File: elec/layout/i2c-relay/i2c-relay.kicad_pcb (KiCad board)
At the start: 2 copper layers, 7 parts, among them U2 10kΩ ±1% 62.5mW, U3 1kΩ ±1% 62.5mW

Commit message: Build everything with ordered params to fix frozen builds
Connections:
- net RESET renamed VCCP
- Q1 pad 2: gnd -> gnd-2
- U1 pad 10: gpio_expander-net-5 -> gpio_expander-net-3
- U1 pad 17: gnd-2 -> gnd
- U1 pad 3: gpio_expander-net-1 -> gpio_expander-net-2
- U1 pad 4: gpio_expander-net-6 -> gpio_expander-net
- U1 pad 5: gpio_expander-net -> gpio_expander-net-6
- U1 pad 6: gnd-2 -> gnd
- U1 pad 7: gpio_expander-net-3 -> gpio_expander-net-5
- U1 pad 9: gpio_expander-net-2 -> gpio_expander-net-1
- U3 pad 2: gnd -> gnd-2
- U4 pad 2: hv -> hv-1
- U6 pad 1: hv -> hv-1
- U6 pad 5: hv-1 -> hv-2
- U6 pad 6: hv-2 -> hv
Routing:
- net hv-1: track 0.00 -> 2.39 mm
- net hv: track 2.39 -> 0.00 mm
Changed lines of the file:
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@@
     )
     (net 0 "")
-    (net 1 "gpio_expander-net-6")
+    (net 1 "gpio_expander-net")
     (net 2 "SCL")
-    (net 3 "gpio_expander-net-5")
-    (net 4 "hv-2")
-    (net 5 "gpio_expander-net-3")
-    (net 6 "gpio_expander-net-2")
-    (net 7 "hv")
+    (net 3 "gpio_expander-net-3")
+    (net 4 "hv")
+    (net 5 "gpio_expander-net-5")
+    (net 6 "gpio_expander-net-1")
+    (net 7 "hv-1")
     (net 8 "line")
     (net 9 "gnd-1")
     (net 10 "INT")
     (net 11 "gpio_expander-net-4")
-    (net 12 "RESET")
-    (net 13 "hv-1")
+    (net 12 "VCCP")
+    (net 13 "hv-2")
     (net 14 "SDA")
-    (net 15 "gpio_expander-net")
+    (net 15 "gpio_expander-net-6")
     (net 16 "gnd-3")
-    (net 17 "gnd")
+    (net 17 "gnd-2")
     (net 18 "gate")
-    (net 19 "gpio_expander-net-1")
-    (net 20 "gnd-2")
+    (net 19 "gpio_expander-net-2")
+    (net 20 "gnd")
     (net 21 "relay-gnd")
     (net 22 "cathode")
@@
             )
         )
+        (property "PARAM_max_power" "{\"type\": \"Quantity_Set_Discrete\", \"data\": {\"intervals\": {\"type\": \"Numeric_Interval_Disjoint\", \"data\": {\"intervals\": [{\"type\": \"Numeric_Interval\", \"data\": {\"min\": 0.0625, \"max\": 0.0625}}]}}, \"unit\": \"watt\"}}"
+            (at 0 0 0)
+            (layer "User.9")
+            (hide yes)
+            (effects
+                (font
+                    (size 0.125 0.125)
+                    (thickness 0.01875)
+                )
+            )
+        )
+        (property "PARAM_max_voltage" "{\"type\": \"Quantity_Set_Discrete\", \"data\": {\"intervals\": {\"type\": \"Numeric_Interval_Disjoint\", \"data\": {\"intervals\": [{\"type\": \"Numeric_Interval\", \"data\": {\"min\": 50.0, \"max\": 50.0}}]}}, \"unit\": \"volt\"}}"
+            (at 0 0 0)
+            (layer "User.9")
+            (hide yes)
+            (effects
+                (font
+                    (size 0.125 0.125)
+                    (thickness 0.01875)
+                )
+            )
+        )
+        (property "PARAM_resistance" "{\"type\": \"Quantity_Interval_Disjoint\", \"data\": {\"intervals\": {\"type\": \"Numeric_Interval_Disjoint\", \"data\": {\"intervals\": [{\"type\": \"Numeric_Interval\", \"data\": {\"min\": 990.0000002235174, \"max\": 1009.9999997764826}}]}}, \"unit\": \"ohm\"}}"
+            (at 0 0 0)
+            (layer "User.9")
+            (hide yes)
+            (effects
+                (font
+                    (size 0.125 0.125)
+                    (thickness 0.01875)
+                )
+            )
+        )
         (attr smd)
         (fp_line
@@
             (size 0.57 0.54)
             (layers "F.Cu" "F.Mask" "F.Paste")
-            (net 17 "gnd")
+            (net 17 "gnd-2")
             (remove_unused_layers yes)
             (keep_end_layers yes)
@@
             (size 0.8 0.8)
             (layers "F.Cu" "F.Mask" "F.Paste")
-            (net 7 "hv")
+            (net 7 "hv-1")
             (remove_unused_layers yes)
             (keep_end_layers yes)
@@
             (drill 0.999998)
             (layers "*.Cu" "*.Mask")
-            (net 7 "hv")
+            (net 7 "hv-1")
             (remove_unused_layers no)
             (keep_end_layers yes)
@@
             (drill 0.999998)
             (layers "*.Cu" "*.Mask")
-            (net 13 "hv-1")
+            (net 13 "hv-2")
             (remove_unused_layers no)
             (keep_end_layers yes)
@@
             (drill 0.999998)
             (layers "*.Cu" "*.Mask")
-            (net 4 "hv-2")
+            (net 4 "hv")
             (remove_unused_layers no)
             (keep_end_layers yes)
@@
             )
         )
+        (property "PARAM_max_power" "{\"type\": \"Quantity_Set_Discrete\", \"data\": {\"intervals\": {\"type\": \"Numeric_Interval_Disjoint\", \"data\": {\"intervals\": [{\"type\": \"Numeric_Interval\", \"data\": {\"min\": 0.0625, \"max\": 0.0625}}]}}, \"unit\": \"watt\"}}"
+            (at 0 0 0)
+            (layer "User.9")
+            (hide yes)
+            (effects
+                (font
+                    (size 0.125 0.125)
+                    (thickness 0.01875)
+                )
+            )
+        )
+        (property "PARAM_resistance" "{\"type\": \"Quantity_Interval_Disjoint\", \"data\": {\"intervals\": {\"type\": \"Numeric_Interval_Disjoint\", \"data\": {\"intervals\": [{\"type\": \"Numeric_Interval\", \"data\": {\"min\": 990.0000002235174, \"max\": 1009.9999997764826}}]}}, \"unit\": \"ohm\"}}"
+            (at 0 0 0)
+            (layer "User.9")
+            (hide yes)
+            (effects
+                (font
+                    (size 0.125 0.125)
+                    (thickness 0.01875)
+                )
+            )
+        )
+        (property "PARAM_max_voltage" "{\"type\": \"Quantity_Set_Discrete\", \"data\": {\"intervals\": {\"type\": \"Numeric_Interval_Disjoint\", \"data\": {\"intervals\": [{\"type\": \"Numeric_Interval\", \"data\": {\"min\": 50.0, \"max\": 50.0}}]}}, \"unit\": \"volt\"}}"
+            (at 0 0 0)
+            (layer "User.9")
+            (hide yes)
+            (effects
+                (font
+                    (size 0.125 0.125)
+                    (thickness 0.01875)
+                )
+            )
+        )
         (attr smd)
         (fp_line
@@
             (size 1.07 0.6)
             (layers "F.Cu" "F.Paste" "F.Mask")
-            (net 17 "gnd")
+            (net 17 "gnd-2")
             (remove_unused_layers yes)
             (keep_end_layers yes)
@@
             (size 0.28 0.66)
             (layers "F.Cu" "F.Mask" "F.Paste")
-            (net 12 "RESET")
+            (net 12 "VCCP")
             (remove_unused_layers yes)
             (keep_end_layers yes)
@@
             (size 0.28 0.66)
             (layers "F.Cu" "F.Mask" "F.Paste")
-            (net 19 "gpio_expander-net-1")
+            (net 19 "gpio_expander-net-2")
             (remove_unused_layers yes)
             (keep_end_layers yes)
@@
             (size 0.28 0.66)
             (layers "F.Cu" "F.Mask" "F.Paste")
-            (net 1 "gpio_expander-net-6")
+            (net 1 "gpio_expander-net")
             (remove_unused_layers yes)
             (keep_end_layers yes)
@@
             (size 0.66 0.28)
             (layers "F.Cu" "F.Mask" "F.Paste")
-            (net 15 "gpio_expander-net")
+            (net 15 "gpio_expander-net-6")
             (remove_unused_layers yes)
             (keep_end_layers yes)
@@
             (size 0.66 0.28)
             (layers "F.Cu" "F.Mask" "F.Paste")
-            (net 20 "gnd-2")
+            (net 20 "gnd")
             (remove_unused_layers yes)
             (keep_end_layers yes)
@@
             (size 0.66 0.28)
             (layers "F.Cu" "F.Mask" "F.Paste")
-            (net 5 "gpio_expander-net-3")
+            (net 5 "gpio_expander-net-5")
             (remove_unused_layers yes)
             (keep_end_layers yes)
@@
             (size 0.28 0.66)
             (layers "F.Cu" "F.Mask" "F.Paste")
-            (net 6 "gpio_expander-net-2")
+            (net 6 "gpio_expander-net-1")
             (remove_unused_layers yes)
             (keep_end_layers yes)
@@
             (size 0.28 0.66)
             (layers "F.Cu" "F.Mask" "F.Paste")
-            (net 3 "gpio_expander-net-5")
+            (net 3 "gpio_expander-net-3")
             (remove_unused_layers yes)
             (keep_end_layers yes)
@@
             (size 0.66 0.28)
             (layers "F.Cu" "F.Mask" "F.Paste")
-            (net 12 "RESET")
+            (net 12 "VCCP")
             (remove_unused_layers yes)
             (keep_end_layers yes)
@@
             (size 0.66 0.28)
             (layers "F.Cu" "F.Mask" "F.Paste")
-            (net 12 "RESET")
+            (net 12 "VCCP")
             (remove_unused_layers yes)
             (keep_end_layers yes)
@@
             (size 1.75 1.75)
             (layers "F.Cu" "F.Mask" "F.Paste")
-            (net 20 "gnd-2")
+            (net 20 "gnd")
             (remove_unused_layers yes)
             (keep_end_layers yes)
@@
             (at 0 0 0)
             (layer "User.9")
+            (hide yes)
+            (effects
+                (font
+                    (size 0.125 0.125)
+                    (thickness 0.01875)
+                )
+            )
+        )
+        (property "PARAM_max_power" "{\"type\": \"Quantity_Set_Discrete\", \"data\": {\"intervals\": {\"type\": \"Numeric_Interval_Disjoint\", \"data\": {\"intervals\": [{\"type\": \"Numeric_Interval\", \"data\": {\"min\": 0.0625, \"max\": 0.0625}}]}}, \"unit\": \"watt\"}}"
+            (at 0 0 0)
+            (layer "User.9")
+            (hide yes)
+            (effects
+                (font
+                    (size 0.125 0.125)
+                    (thickness 0.01875)
+                )
+            )
+        )
+        (property "PARAM_max_voltage" "{\"type\": \"Quantity_Set_Discrete\", \"data\": {\"intervals\": {\"type\": \"Numeric_Interval_Disjoint\", \"data\": {\"intervals\": [{\"type\": \"Numeric_Interval\", \"data\": {\"min\": 50.0, \"max\": 50.0}}]}}, \"unit\": \"volt\"}}"
+            (at 0 0 0)
+            (layer "User.9")
+            (hide yes)
+            (effects
+                (font
+                    (size 0.125 0.125)
+                    (thickness 0.01875)
+                )
+            )
+        )
+        (property "PARAM_resistance" "{\"type\": \"Quantity_Interval_Disjoint\", \"data\": {\"intervals\": {\"type\": \"Numeric_Interval_Disjoint\", \"data\": {\"intervals\": [{\"type\": \"Numeric_Interval\", \"data\": {\"min\": 9900.000002235174, \"max\": 10099.999997764826}}]}}, \"unit\": \"ohm\"}}"
+            (at 0 0 0)
+            (layer "User.9")

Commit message: Cleanup layout for usb hub and usb-uart, add CM5 controller heatsink outline
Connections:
- Q1 pad 2: gnd-2 -> gnd-3
- U1 pad 10: gpio_expander-net-3 -> gpio_expander-net-5
- U1 pad 3: gpio_expander-net-2 -> gpio_expander-net-1
- U1 pad 5: gpio_expander-net-6 -> gpio_expander-net-2
- U1 pad 7: gpio_expander-net-5 -> gpio_expander-net-4
- U1 pad 8: gpio_expander-net-4 -> gpio_expander-net-6
- U1 pad 9: gpio_expander-net-1 -> gpio_expander-net-3
- U3 pad 2: gnd-2 -> gnd-3
- U4 pad 2: hv-1 -> hv
- U6 pad 1: hv-1 -> hv
- U6 pad 3: gnd-1 -> gnd-2
- U6 pad 4: gnd-3 -> gnd-1
- U6 pad 6: hv -> hv-1
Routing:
- net hv-1: track 2.39 -> 0.00 mm
- net hv: track 0.00 -> 2.39 mm
- net gnd-3: track 0.00 -> 1.46 mm
- net gnd-2: track 1.46 -> 0.00 mm
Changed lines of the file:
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@@
     (net 1 "gpio_expander-net")
     (net 2 "SCL")
-    (net 3 "gpio_expander-net-3")
-    (net 4 "hv")
-    (net 5 "gpio_expander-net-5")
-    (net 6 "gpio_expander-net-1")
-    (net 7 "hv-1")
+    (net 3 "gpio_expander-net-5")
+    (net 4 "hv-1")
+    (net 5 "gpio_expander-net-4")
+    (net 6 "gpio_expander-net-3")
+    (net 7 "hv")
     (net 8 "line")
-    (net 9 "gnd-1")
+    (net 9 "gnd-2")
     (net 10 "INT")
-    (net 11 "gpio_expander-net-4")
+    (net 11 "gpio_expander-net-6")
     (net 12 "VCCP")
     (net 13 "hv-2")
     (net 14 "SDA")
-    (net 15 "gpio_expander-net-6")
-    (net 16 "gnd-3")
-    (net 17 "gnd-2")
+    (net 15 "gpio_expander-net-2")
+    (net 16 "gnd-1")
+    (net 17 "gnd-3")
     (net 18 "gate")
-    (net 19 "gpio_expander-net-2")
+    (net 19 "gpio_expander-net-1")
     (net 20 "gnd")
     (net 21 "relay-gnd")
@@
             (size 0.57 0.54)
             (layers "F.Cu" "F.Mask" "F.Paste")
-            (net 17 "gnd-2")
+            (net 17 "gnd-3")
             (remove_unused_layers yes)
             (keep_end_layers yes)
@@
             (size 0.8 0.8)
             (layers "F.Cu" "F.Mask" "F.Paste")
-            (net 7 "hv-1")
+            (net 7 "hv")
             (remove_unused_layers yes)
             (keep_end_layers yes)
@@
             (drill 0.999998)
             (layers "*.Cu" "*.Mask")
-            (net 7 "hv-1")
+            (net 7 "hv")
             (remove_unused_layers no)
             (keep_end_layers yes)
@@
             (drill 0.999998)
             (layers "*.Cu" "*.Mask")
-            (net 9 "gnd-1")
+            (net 9 "gnd-2")
             (remove_unused_layers no)
             (keep_end_layers yes)
@@
             (drill 0.999998)
             (layers "*.Cu" "*.Mask")
-            (net 16 "gnd-3")
+            (net 16 "gnd-1")
             (remove_unused_layers no)
             (keep_end_layers yes)
@@
             (drill 0.999998)
             (layers "*.Cu" "*.Mask")
-            (net 4 "hv")
+            (net 4 "hv-1")
             (remove_unused_layers no)
             (keep_end_layers yes)
@@
             (size 1.07 0.6)
             (layers "F.Cu" "F.Paste" "F.Mask")
-            (net 17 "gnd-2")
+            (net 17 "gnd-3")
             (remove_unused_layers yes)
             (keep_end_layers yes)
@@
             (size 0.28 0.66)
             (layers "F.Cu" "F.Mask" "F.Paste")
-            (net 19 "gpio_expander-net-2")
+            (net 19 "gpio_expander-net-1")
             (remove_unused_layers yes)
             (keep_end_layers yes)
@@
             (size 0.66 0.28)
             (layers "F.Cu" "F.Mask" "F.Paste")
-            (net 15 "gpio_expander-net-6")
+            (net 15 "gpio_expander-net-2")
             (remove_unused_layers yes)
             (keep_end_layers yes)
@@
             (size 0.66 0.28)
             (layers "F.Cu" "F.Mask" "F.Paste")
-            (net 5 "gpio_expander-net-5")
+            (net 5 "gpio_expander-net-4")
             (remove_unused_layers yes)
             (keep_end_layers yes)
@@
             (size 0.66 0.28)
             (layers "F.Cu" "F.Mask" "F.Paste")
-            (net 11 "gpio_expander-net-4")
+            (net 11 "gpio_expander-net-6")
             (remove_unused_layers yes)
             (keep_end_layers yes)
@@
             (size 0.28 0.66)
             (layers "F.Cu" "F.Mask" "F.Paste")
-            (net 6 "gpio_expander-net-1")
+            (net 6 "gpio_expander-net-3")
             (remove_unused_layers yes)
             (keep_end_layers yes)
@@
             (size 0.28 0.66)
             (layers "F.Cu" "F.Mask" "F.Paste")
-            (net 3 "gpio_expander-net-3")
-            (remove_unused_layers yes)
-            (keep_end_layers yes)
+            (net 3 "gpio_expander-net-5")
+            (remove_unused_layers yes)
+            (keep_end_layers yes)

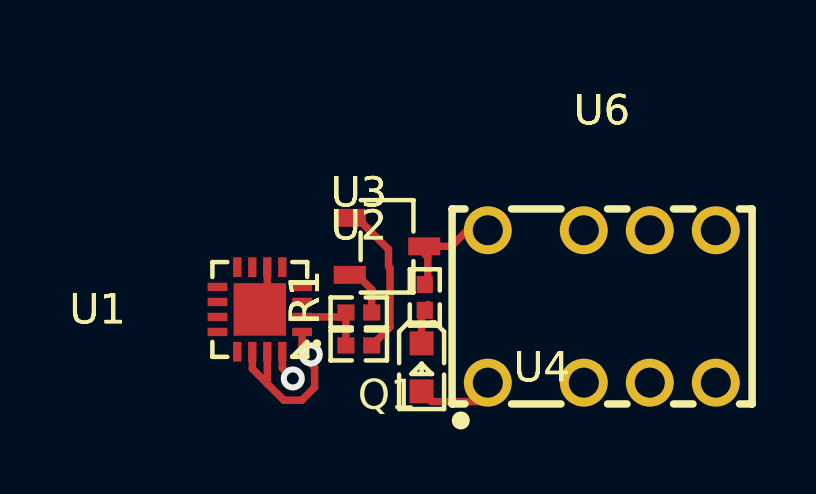
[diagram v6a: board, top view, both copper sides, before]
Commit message: update relay led value
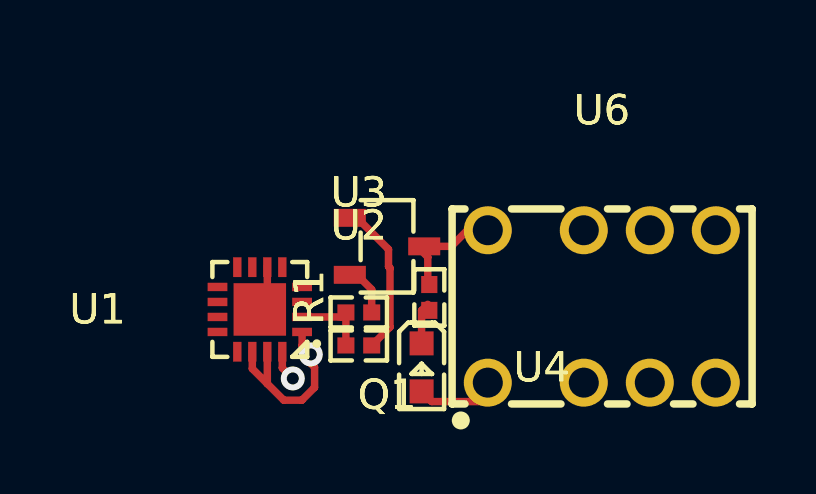
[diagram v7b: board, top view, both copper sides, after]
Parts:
- R1: value 1kΩ ±1% 62.5mW -> 2kΩ ±1% 62.5mW
- moved R1 0.15 mm to (65.7, 27.1)
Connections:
- net VCCP renamed VCCI
- Q1 pad 2: gnd-3 -> gnd
- U1 pad 10: gpio_expander-net-5 -> gpio_expander-net-3
- U1 pad 17: gnd -> gnd-3
- U1 pad 3: gpio_expander-net-1 -> gpio_expander-net-5
- U1 pad 5: gpio_expander-net-2 -> gpio_expander-net-4
- U1 pad 6: gnd -> gnd-3
- U1 pad 7: gpio_expander-net-4 -> gpio_expander-net-6
- U1 pad 8: gpio_expander-net-6 -> gpio_expander-net-1
- U1 pad 9: gpio_expander-net-3 -> gpio_expander-net-2
- U3 pad 2: gnd-3 -> gnd
- U4 pad 2: hv -> hv-1
- U6 pad 1: hv -> hv-1
- U6 pad 3: gnd-2 -> gnd-1
- U6 pad 4: gnd-1 -> gnd-2
- U6 pad 5: hv-2 -> hv
- U6 pad 6: hv-1 -> hv-2
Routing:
- net hv-1: track 0.00 -> 2.39 mm
- net hv: track 2.39 -> 0.00 mm

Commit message: checkin
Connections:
- net VCCI renamed VCCP
- Q1 pad 2: gnd -> gnd-1
- U1 pad 17: gnd-3 -> gnd
- U1 pad 3: gpio_expander-net-5 -> gpio_expander-net-2
- U1 pad 4: gpio_expander-net -> gpio_expander-net-6
- U1 pad 5: gpio_expander-net-4 -> gpio_expander-net-1
- U1 pad 6: gnd-3 -> gnd
- U1 pad 7: gpio_expander-net-6 -> gpio_expander-net-4
- U1 pad 8: gpio_expander-net-1 -> gpio_expander-net
- U1 pad 9: gpio_expander-net-2 -> gpio_expander-net-5
- U3 pad 2: gnd -> gnd-1
- U6 pad 3: gnd-1 -> gnd-3
- U6 pad 5: hv -> hv-2
- U6 pad 6: hv-2 -> hv
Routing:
- net gnd-3: track 1.51 -> 0.00 mm
- net gnd-1: track 0.00 -> 1.46 mm
